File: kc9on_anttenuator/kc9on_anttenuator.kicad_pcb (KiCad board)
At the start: 2 copper layers, 39.4 x 35.6 mm, 21 parts, among them J1 9v Battery, J2 Antenna, J3 Radio, Q1 J113, SW1 OS102011MA1QS1, Y1 4.000MHz

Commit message: delete is all and start again
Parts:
- removed the D1 at (135.4, 62.0)
- removed G***: LOGO, LOGO
- removed J2: Antenna, BNC:CONN_73100-0105_MOL
- removed J3: Radio, BNC:CONN_73100-0105_MOL
- removed RV2: 20K, Potentiometer_THT:Potentiometer_Bourns_3386F_Vertical
- added D1: 5mm, LED_THT:LED_D5.0mm, F.Cu at (96.5, 183.7)
- added D1: 5mm, LED_SMD:LED_1206_3216Metric, F.Cu at (80.5, 184.1)
- added R6: 4.7K, Resistor_SMD:R_1206_3216Metric, F.Cu at (74.8, 176.7)
- SW1: footprint BNC:SWITCH_11MA1QS1 -> Atten:SWITCH_11MA1QS1
- moved J1 131.1 mm to (79.9, 177.5)
- moved R4 125.0 mm to (74.8, 170.1), turned to 0 degrees
- moved RV1 124.1 mm to (84.9, 168.4), turned to 0 degrees
- moved R5 123.8 mm to (74.8, 173.4), turned to 0 degrees
- moved Q1 122.8 mm to (74.6, 180.6)
- moved D2 121.4 mm to (84.8, 181.8)
- moved C4 119.7 mm to (80.4, 170.2), turned to 0 degrees
- moved C3 119.3 mm to (80.4, 166.9), turned to 0 degrees
- moved SW1 117.5 mm to (63.4, 161.4), turned to 0 degrees
- moved R2 115.1 mm to (74.8, 163.5), turned to 0 degrees
- moved R1 114.0 mm to (74.8, 160.2), turned to 0 degrees
- moved C2 109.7 mm to (80.4, 163.5), turned to 0 degrees
- moved C5 105.2 mm to (80.4, 173.6), turned to 0 degrees
- moved Y1 103.4 mm to (87.4, 176.6), turned to 0 degrees
- moved R3 98.7 mm to (74.8, 166.8), turned to 0 degrees
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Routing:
- net Net-(J2-Ext): track 32.9 -> 0.00 mm
- net Net-(Q1-S): track 30.4 -> 0.00 mm, vias 2 -> 0
- net Net-(Q1-G): track 17.4 -> 0.00 mm
- net Net-(SW1-C): track 16.1 -> 0.00 mm
- net Net-(R6-Pad1): track 15.6 -> 0.00 mm
- net Net-(Q1-D): track 15.0 -> 0.00 mm
- net Net-(D2-A): track 9.74 -> 0.00 mm
- net Net-(J1-Pin_2): track 8.68 -> 0.00 mm
- net Net-(D2-K): track 8.12 -> 0.00 mm
- net Net-(D1-A): track 7.26 -> 0.00 mm
- net Net-(J2-In): track 6.66 -> 0.00 mm
- net Net-(R4-Pad1): track 4.84 -> 0.00 mm
- net Net-(J3-In): track 2.86 -> 0.00 mm
- net GND: vias 173 -> 0
- removed copper zone on B.Cu, net GND
- removed copper zone on F.Cu, net GND
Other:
- board outline removed
- board text removed: "+"
- board text removed: "9v Bat"
- board text removed: "ANTENNA"
- board text removed: "FoxHunt Offset Attenuator v1"
- board text removed: "Grilled Cheese Engineering 2026 Original Design by John KC9ON Updated & Adapted by Josh KK6JDC"
- board text removed: "RADIO"

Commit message: started version 1
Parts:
- added J2: Antenna, Atten:CONN_73100-0105_MOL, F.Cu at (157.0, 83.0)
- added J3: Radio, Atten:CONN_73100-0105_MOL, F.Cu at (157.0, 118.0)
- C2: value 220pF -> 15pf
- Q1: value J113 -> MMBF5457
- R6: value 4.7K -> 2.2K
- RV1: footprint Potentiometer_THT:Potentiometer_Bourns_PTV09A-1_Single_Vertical -> Atten:TRIM_PT01-D225D-B103
- SW1: value OS102011MA1QS1 -> SW_SPDT
- moved R5 121.7 mm to (160.8, 87.2), turned to 90 degrees
- moved D2 117.6 mm to (160.8, 92.0), turned to 180 degrees
- moved Q1 116.6 mm to (167.2, 109.8), turned to 90 degrees
- moved C4 112.9 mm to (157.0, 87.2), turned to 90 degrees
- moved Y1 108.8 mm to (167.2, 102.7), turned to 90 degrees
- moved C3 107.9 mm to (153.2, 87.2), turned to 90 degrees
- moved RV1 100.0 mm to (157.0, 99.0)
- moved C2 99.8 mm to (167.2, 114.2)
- moved D1 99.3 mm to (146.5, 98.0), turned to -90 degrees
- moved SW1 93.7 mm to (144.8, 114.7), turned to -90 degrees
- moved R2 92.5 mm to (146.5, 105.0)
- moved R1 88.2 mm to (146.5, 108.8)
- moved J1 85.2 mm to (148.3, 126.8), turned to -90 degrees
- moved C1 83.2 mm to (150.0, 114.5), turned to 90 degrees
- moved R3 78.5 mm to (104.2, 94.0)
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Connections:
- RV1 pad MP: (no net) -> GND
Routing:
- net Net-(Q1-D): track 0.00 -> 17.5 mm
- net Net-(J1-Pin_2): track 0.00 -> 11.6 mm
- net Net-(Q1-G): track 0.00 -> 5.92 mm
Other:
- board outline added: 30 x 60 mm

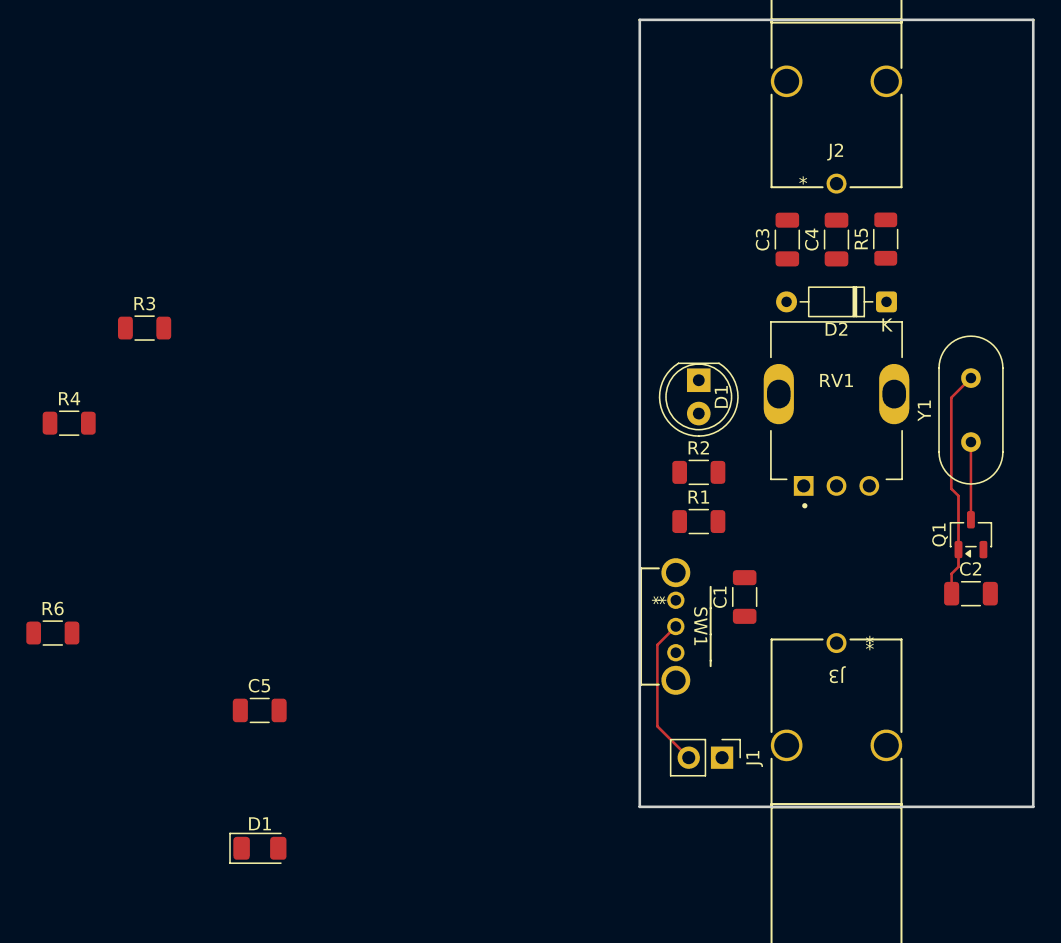
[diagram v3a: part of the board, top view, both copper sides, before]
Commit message: putting a hold on SMD for now. gonna switch to tht
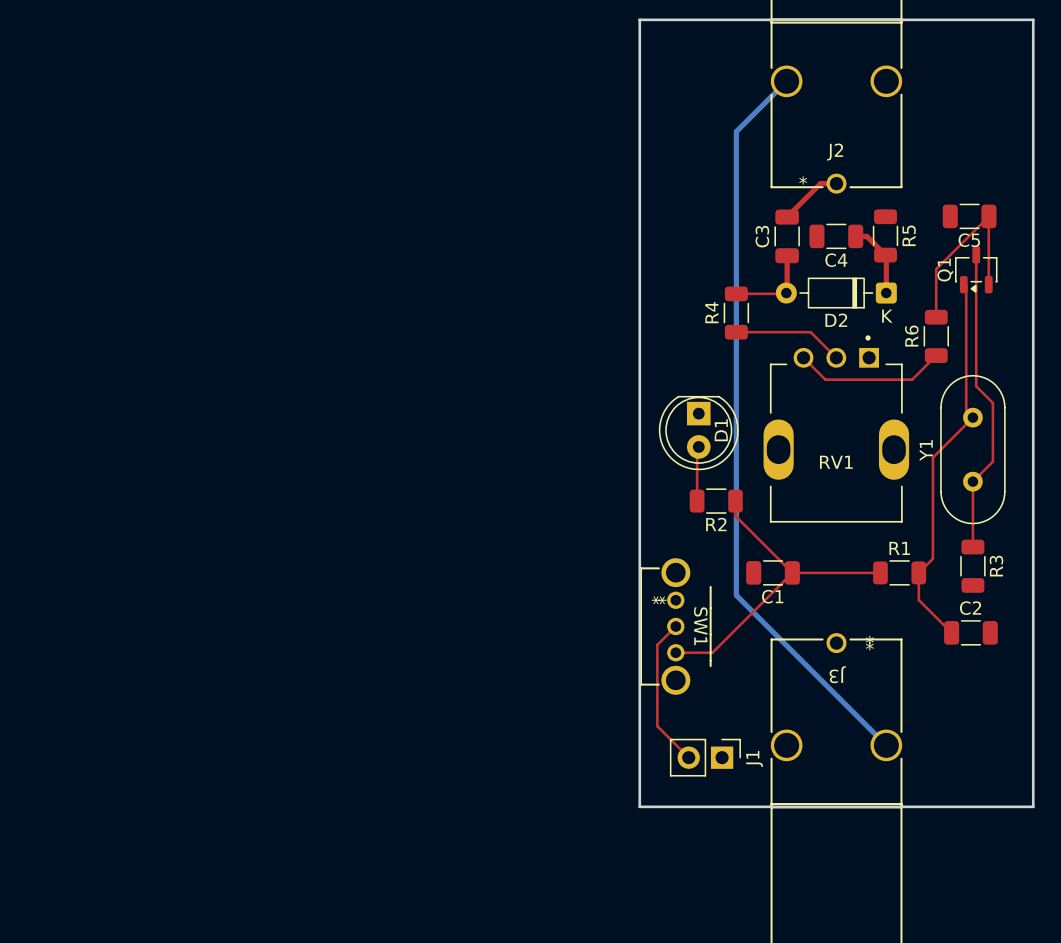
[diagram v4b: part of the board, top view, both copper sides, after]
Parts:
- removed the D1 at (113.0, 133.7)
- moved R6 71.1 mm to (164.6, 94.6), turned to 90 degrees
- moved C5 65.9 mm to (167.1, 85.5), turned to 180 degrees
- moved R3 65.7 mm to (167.4, 112.2), turned to -90 degrees
- moved R4 51.6 mm to (149.4, 92.9), turned to 90 degrees
- moved Q1 20.2 mm to (167.7, 89.5)
- moved R1 15.8 mm to (161.8, 112.7)
- moved RV1 4.24 mm to (157.0, 103.3), turned to 180 degrees
- moved Y1 3.02 mm to (167.4, 105.7)
- moved C2 2.99 mm to (167.2, 117.2)
- moved C1 2.83 mm to (152.2, 112.7), turned to 180 degrees
- moved R2 2.57 mm to (147.8, 107.2), turned to 180 degrees
- moved D1 2.55 mm to (146.5, 100.5)
- moved D2 0.67 mm to (160.8, 91.3)
- moved R5 0.24 mm to (160.7, 87.0), turned to -90 degrees
- moved C3 0.24 mm to (153.2, 87.0)
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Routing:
- net Net-(J2-Ext): track 0.00 -> 57.0 mm
- net Net-(SW1-C): track 0.00 -> 25.4 mm
- net Net-(Q1-G): track 5.92 -> 23.4 mm
- net Net-(Q1-S): track 0.00 -> 14.6 mm
- net Net-(Q1-D): track 17.5 -> 29.6 mm
- net Net-(R6-Pad1): track 0.00 -> 11.6 mm
- net Net-(R4-Pad1): track 0.00 -> 8.43 mm
- net Net-(D2-A): track 0.00 -> 6.70 mm
- net Net-(D2-K): track 0.00 -> 5.78 mm
- net Net-(J2-In): track 0.00 -> 4.82 mm
- net Net-(D1-A): track 0.00 -> 4.18 mm

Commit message: Through hole madness
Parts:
- C1, C3, C4, C5: footprint Capacitor_SMD:C_1206_3216Metric -> Capacitor_THT:C_Disc_D4.3mm_W1.9mm_P5.00mm
- C2: value 15pf -> 15pF; footprint Capacitor_SMD:C_1206_3216Metric -> Capacitor_THT:C_Disc_D4.3mm_W1.9mm_P5.00mm
- Q1: value MMBF5457 -> J113; footprint Package_TO_SOT_SMD:SOT-23-3 -> Package_TO_SOT_THT:TO-92L_Inline
- R1, R2, R3, R4, R5: footprint Resistor_SMD:R_1206_3216Metric -> Resistor_THT:R_Axial_DIN0207_L6.3mm_D2.5mm_P7.62mm_Horizontal
- R6: value 2.2K -> 2.2k; footprint Resistor_SMD:R_1206_3216Metric -> Resistor_THT:R_Axial_DIN0207_L6.3mm_D2.5mm_P7.62mm_Horizontal
- moved R3 23.4 mm to (167.4, 88.8), turned to 90 degrees
- moved C5 19.8 mm to (147.3, 84.7), turned to 90 degrees
- moved R6 15.6 mm to (149.1, 96.4)
- moved R1 8.65 mm to (153.2, 112.2)
- moved R2 7.78 mm to (149.9, 114.7), turned to 90 degrees
- moved Q1 5.47 mm to (166.2, 94.8), turned to 0 degrees
- moved C2 5.30 mm to (167.4, 111.9), turned to -90 degrees
- moved R4 5.21 mm to (145.6, 96.4)
- moved R5 4.82 mm to (155.9, 86.5), turned to 0 degrees
- moved C4 4.72 mm to (160.8, 89.8)
- moved C1 3.44 mm to (154.5, 115.2), turned to 0 degrees
- moved C3 3.26 mm to (153.2, 90.3)
- moved D2 1.78 mm to (160.8, 93.1)
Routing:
- net Net-(J3-In): track 0.00 -> 31.3 mm
- net Net-(Q1-S): track 14.6 -> 0.00 mm
- net Net-(SW1-C): track 25.4 -> 14.7 mm
- net Net-(R6-Pad1): track 11.6 -> 5.43 mm
- net Net-(Q1-G): track 23.4 -> 18.0 mm
- net Net-(D2-A): track 6.70 -> 11.1 mm
- net Net-(Q1-D): track 29.6 -> 25.4 mm
- net Net-(R4-Pad1): track 8.43 -> 12.4 mm
- net Net-(D2-K): track 5.78 -> 7.72 mm
- net Net-(D1-A): track 4.18 -> 5.41 mm

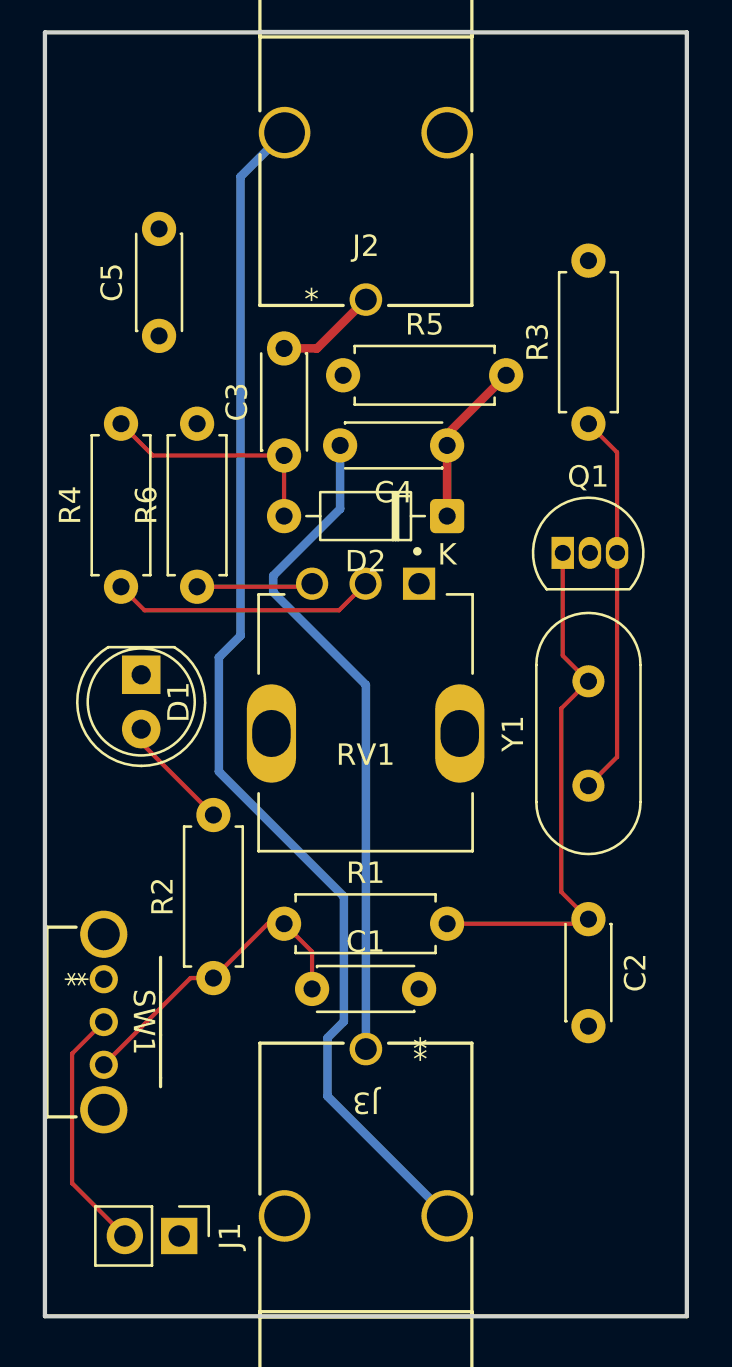
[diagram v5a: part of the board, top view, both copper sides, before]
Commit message: Revert "Through hole madness"
This reverts commit a7be0a8d3e6160941e8986d512c69c6a5ee37fb8.
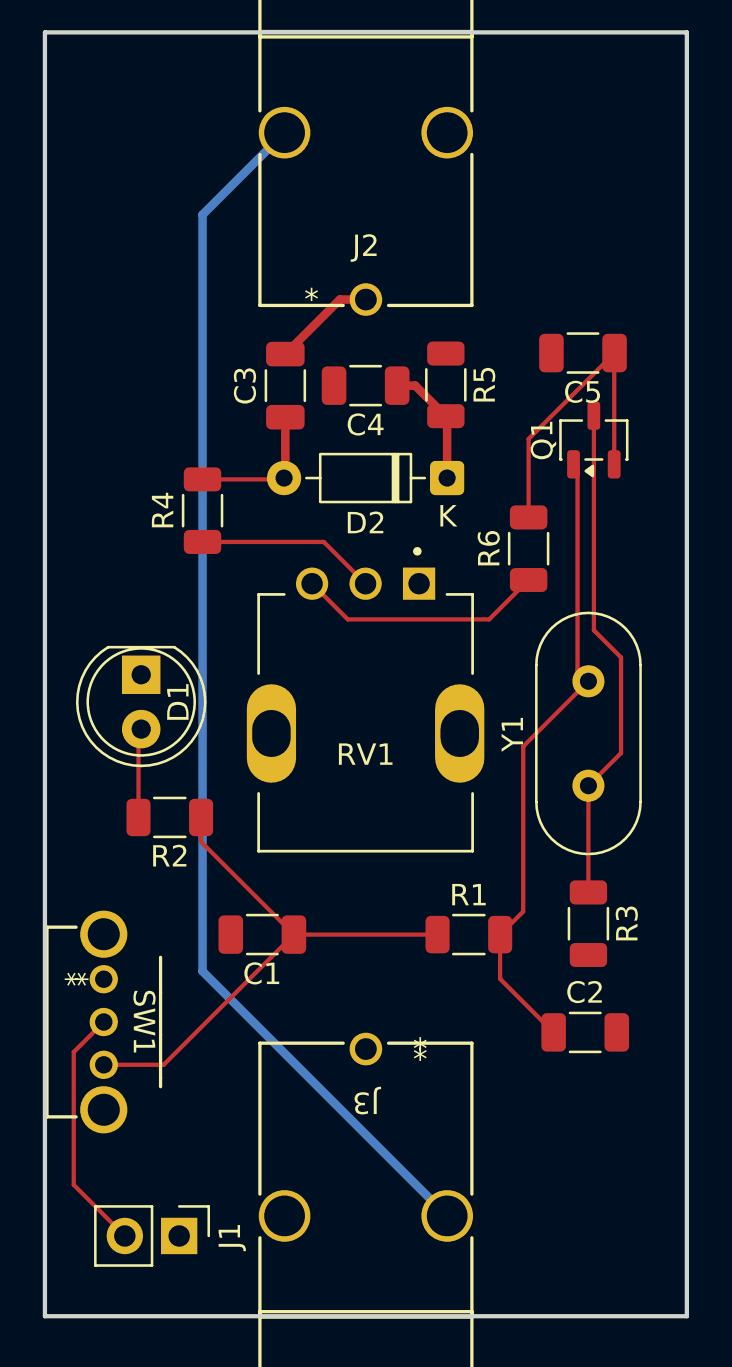
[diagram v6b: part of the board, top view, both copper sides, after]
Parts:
- C1, C3, C4, C5: footprint Capacitor_THT:C_Disc_D4.3mm_W1.9mm_P5.00mm -> Capacitor_SMD:C_1206_3216Metric
- C2: value 15pF -> 15pf; footprint Capacitor_THT:C_Disc_D4.3mm_W1.9mm_P5.00mm -> Capacitor_SMD:C_1206_3216Metric
- Q1: value J113 -> MMBF5457; footprint Package_TO_SOT_THT:TO-92L_Inline -> Package_TO_SOT_SMD:SOT-23-3
- R1, R2, R3, R4, R5: footprint Resistor_THT:R_Axial_DIN0207_L6.3mm_D2.5mm_P7.62mm_Horizontal -> Resistor_SMD:R_1206_3216Metric
- R6: value 2.2k -> 2.2K; footprint Resistor_THT:R_Axial_DIN0207_L6.3mm_D2.5mm_P7.62mm_Horizontal -> Resistor_SMD:R_1206_3216Metric
- moved R3 23.4 mm to (167.4, 112.2), turned to -90 degrees
- moved C5 19.8 mm to (167.1, 85.5), turned to 180 degrees
- moved R6 15.6 mm to (164.6, 94.6)
- moved R1 8.65 mm to (161.8, 112.7)
- moved R2 7.78 mm to (147.8, 107.2), turned to 180 degrees
- moved Q1 5.47 mm to (167.7, 89.5), turned to 90 degrees
- moved C2 5.30 mm to (167.2, 117.2), turned to 0 degrees
- moved R4 5.21 mm to (149.4, 92.9)
- moved R5 4.82 mm to (160.7, 87.0), turned to -90 degrees
- moved C4 4.72 mm to (157.0, 87.0)
- moved C1 3.44 mm to (152.2, 112.7), turned to 180 degrees
- moved C3 3.26 mm to (153.2, 87.0)
- moved D2 1.78 mm to (160.8, 91.3)
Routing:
- net Net-(J3-In): track 31.3 -> 0.00 mm
- net Net-(Q1-S): track 0.00 -> 14.6 mm
- net Net-(SW1-C): track 14.7 -> 25.4 mm
- net Net-(R6-Pad1): track 5.43 -> 11.6 mm
- net Net-(Q1-G): track 18.0 -> 23.4 mm
- net Net-(D2-A): track 11.1 -> 6.70 mm
- net Net-(Q1-D): track 25.4 -> 29.6 mm
- net Net-(R4-Pad1): track 12.4 -> 8.43 mm
- net Net-(D2-K): track 7.72 -> 5.78 mm
- net Net-(D1-A): track 5.41 -> 4.18 mm
